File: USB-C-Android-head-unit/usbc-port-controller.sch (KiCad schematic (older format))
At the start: 5 parts

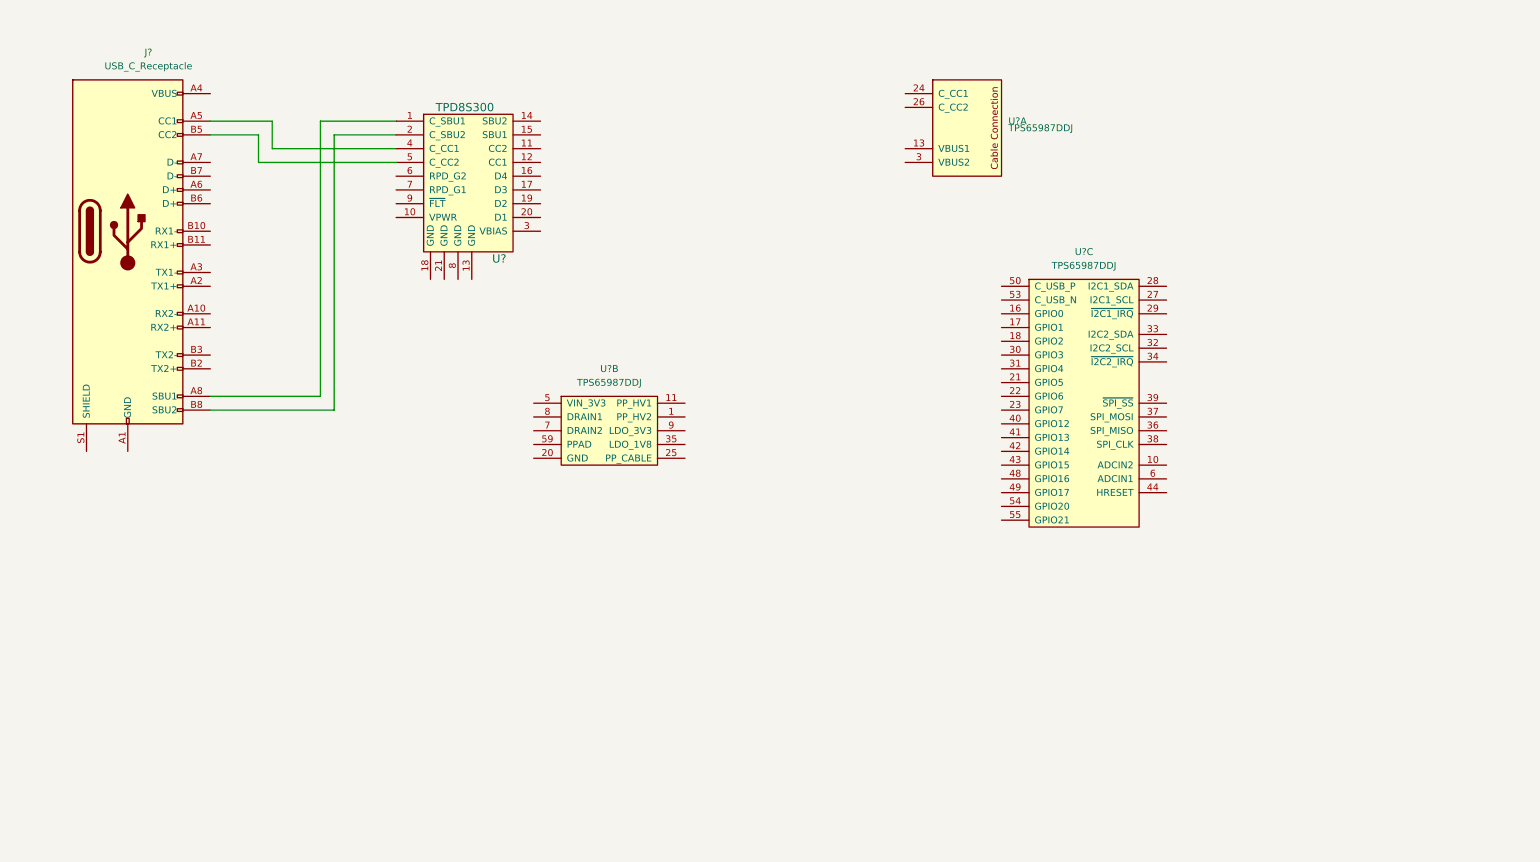
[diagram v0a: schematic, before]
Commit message: starting usb c design
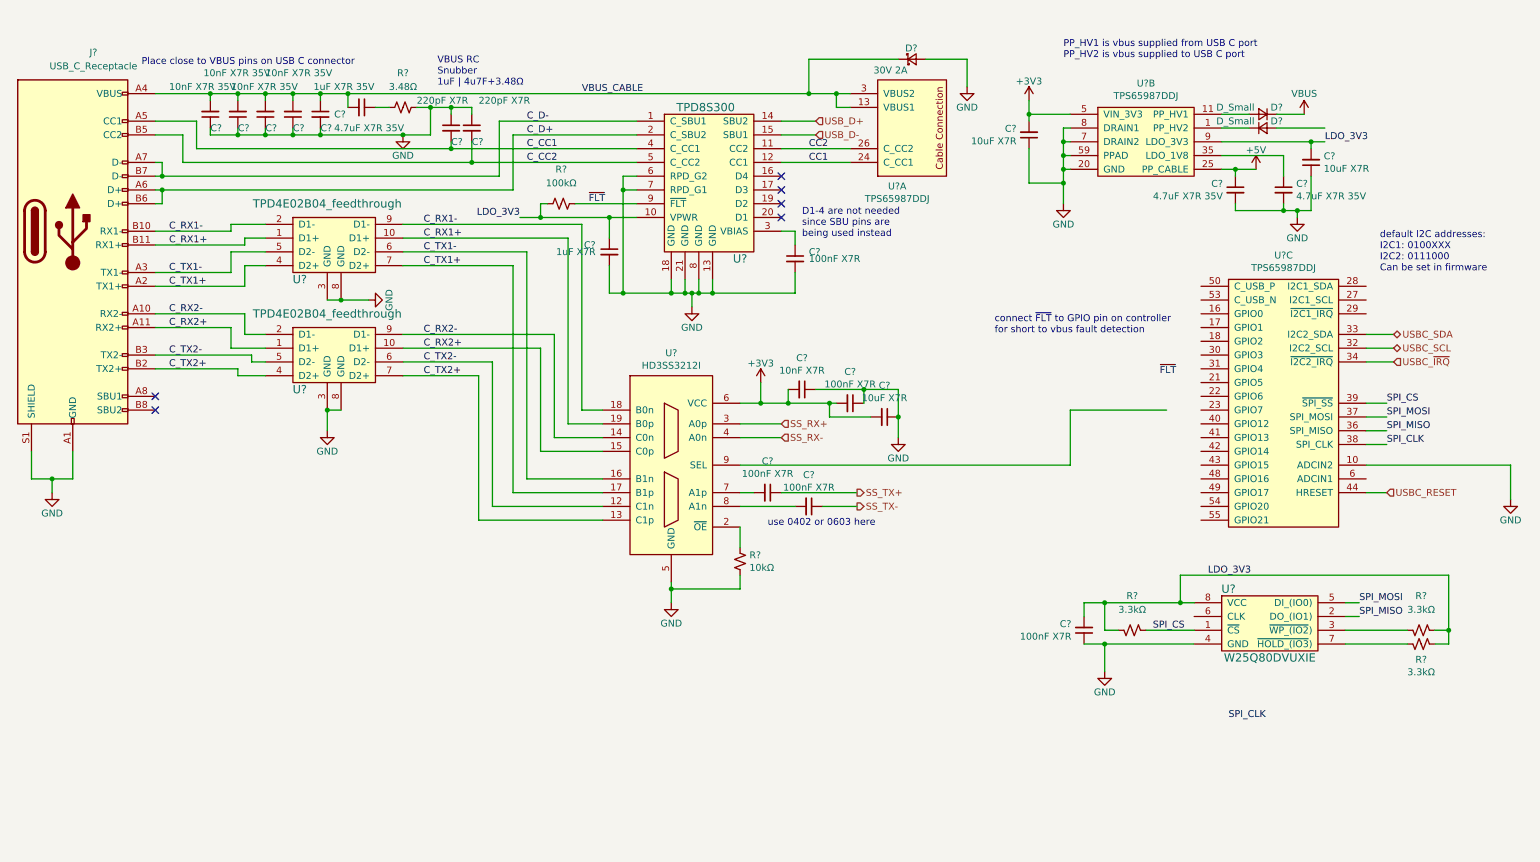
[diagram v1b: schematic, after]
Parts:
- added C? (x5): 100nF X7R, symbol Device:C_Small
- added C?: 1uF X7R, symbol Device:C_Small
- added C?: 10nF X7R, symbol Device:C_Small
- added C? (x3): 10uF X7R, symbol Device:C_Small
- added C? (x4): 10nF X7R 35V, symbol Device:C_Small
- added C?: 1uF X7R 35V, symbol Device:C_Small
- added C? (x3): 4.7uF X7R 35V, symbol Device:C_Small
- added C? (x2): 220pF X7R, symbol Device:C_Small
- added D? (x2): D_Small, symbol Device:D_Small
- added D?: 30V 2A, symbol Device:D_Schottky_Small
- added R?: 100kΩ, symbol Device:R_Small_US
- added R?: 10kΩ, symbol Device:R_Small_US
- added R?: 3.48Ω, symbol Device:R_Small_US
- added R? (x3): 3.3kΩ, symbol Device:R_Small_US
- added U? (x2): TPD4E02B04_feedthrough, Package_SON:USON-10_2.5x1.0mm_P0.5mm, symbol SW-Texas:TPD4E02B04_feedthrough
- added U?: HD3SS3212I, symbol SW-Texas:HD3SS3212I
- added U?: W25Q80DVUXIE, Package_SON:SON-8-1EP_3x2mm_P0.5mm_EP1.4x1.6mm, symbol SW-Winbond:W25Q80DVUXIE
- J?: MPN (none) -> UJ31-CH-3-SMT-TR; Manufacturer (none) -> CUI Inc
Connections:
- net GND: now reaches J?.A1 (GND), J?.A12 (GND), J?.B1 (GND), J?.B12 (GND)
- net GND: now also J?.S1 (SHIELD), U?.10 (ADCIN2), U?.13 (GND), U?.15 (DRAIN1), U?.18 (GND), U?.19 (DRAIN1), U?.20 (GND), U?.21 (GND), U?.45 (GND), U?.46 (GND), U?.47 (GND), U?.51 (GND), U?.52 (DRAIN2), U?.56 (DRAIN2), U?.57 (DRAIN2), U?.58 (DRAIN1), U?.59 (PPAD), U?.6 (RPD_G2), U?.7 (DRAIN2), U?.7 (RPD_G1), U?.8 (DRAIN1), U?.8 (GND), C?.1, C?.1, C?.1, C?.1, C?.1, C?.1, C?.1, C?.1, C?.1, C?.1, C?.1, C?.1, C?.2, C?.2, C?.2, C?.2, C?.2, D?.2 (A), R?.2, R?.2, U?.11 (GND), U?.20 (GND), U?.3 (GND), U?.3 (GND), U?.4 (GND), U?.5 (GND), U?.8 (GND), U?.8 (GND)
- net C_RX2-: now reaches J?.A10 (RX2-)
- net C_RX2-: now also U?.14 (C0n), U?.2 (D1-), U?.9 (D1-)
- net C_RX2+: now reaches J?.A11 (RX2+)
- net C_RX2+: now also U?.1 (D1+), U?.10 (D1+), U?.15 (C0p)
- net C_TX1+: now reaches J?.A2 (TX1+)
- net C_TX1+: now also U?.17 (B1p), U?.4 (D2+), U?.7 (D2+)
- net C_TX1-: now reaches J?.A3 (TX1-)
- net C_TX1-: now also U?.16 (B1n), U?.5 (D2-), U?.6 (D2-)
- net VBUS_CABLE: now reaches J?.A4 (VBUS), J?.A9 (VBUS), J?.B4 (VBUS), J?.B9 (VBUS)
- net VBUS_CABLE: now also U?.13 (VBUS1), U?.14 (VBUS1), U?.3 (VBUS2), U?.4 (VBUS2), C?.1, C?.2, C?.2, C?.2, C?.2, C?.2, D?.1 (K)
- net C_CC1: now reaches J?.A5 (CC1), U?.4 (C_CC1)
- net C_CC1: now also C?.2
- net C_D+: now reaches J?.A6 (D+)
- net C_D+: now also J?.B6 (D+), U?.2 (C_SBU2)
- net C_D-: now reaches J?.A7 (D-)
- net C_D-: now also J?.B7 (D-), U?.1 (C_SBU1)
- net at J?.A8 (SBU1): no longer U?.1 (C_SBU1)
- net C_RX1-: now reaches J?.B10 (RX1-)
- net C_RX1-: now also U?.18 (B0n), U?.2 (D1-), U?.9 (D1-)
- net C_RX1+: now reaches J?.B11 (RX1+)
- net C_RX1+: now also U?.1 (D1+), U?.10 (D1+), U?.19 (B0p)
- net C_TX2+: now reaches J?.B2 (TX2+)
- net C_TX2+: now also U?.13 (C1p), U?.4 (D2+), U?.7 (D2+)
- net C_TX2-: now reaches J?.B3 (TX2-)
- net C_TX2-: now also U?.12 (C1n), U?.5 (D2-), U?.6 (D2-)
- net C_CC2: now reaches J?.B5 (CC2), U?.5 (C_CC2)
- net C_CC2: now also C?.2
- net at J?.B8 (SBU2): no longer U?.2 (C_SBU2)
- net CC1: now reaches U?.24 (C_CC1)
- net CC1: now also U?.12 (CC1)
- net CC2: now reaches U?.26 (C_CC2)
- net CC2: now also U?.11 (CC2)
- net at U?.1 (PP_HV2), U?.2 (PP_HV2): now also D?.1 (K)
- net at U?.11 (PP_HV1), U?.12 (PP_HV1): now also D?.2 (A)
- net +5V: now reaches U?.25 (PP_CABLE)
- net +5V: now also C?.1
- net at U?.35 (LDO_1V8): now also C?.1
- net +3V3: now reaches U?.5 (VIN_3V3)
- net +3V3: now also C?.2, C?.2, C?.2, C?.2, U?.6 (VCC)
- net LDO_3V3: now reaches U?.9 (LDO_3V3)
- net LDO_3V3: now also U?.10 (VPWR), C?.1, C?.2, C?.2, R?.1, R?.2, R?.2, R?.2, U?.8 (VCC)
- net USBC_SCL: now reaches U?.32 (I2C2_SCL)
- net USBC_SDA: now reaches U?.33 (I2C2_SDA)
- net USBC_~IRQ: now reaches U?.34 (~I2C2_IRQ)
- net SPI_MISO: now reaches U?.36 (SPI_MISO)
- net SPI_MISO: now also U?.2 (DO_(IO1))
- net SPI_MOSI: now reaches U?.37 (SPI_MOSI)
- net SPI_MOSI: now also U?.5 (DI_(IO0))
- net SPI_CLK: now reaches U?.38 (SPI_CLK)
- net SPI_CS: now reaches U?.39 (~SPI_SS)
- net SPI_CS: now also R?.2, U?.1 (~CS)
- net USBC_RESET: now reaches U?.44 (HRESET)
- net USB_D+: now reaches U?.14 (SBU2)
- net USB_D-: now reaches U?.15 (SBU1)
- net at U?.3 (VBIAS): now also C?.1
- net ~FLT: now reaches U?.9 (~FLT)
- net ~FLT: now also R?.1
- new net: R?.1, U?.2 (~OE)
- new net: C?.2, U?.7 (A1p)
- new net: C?.2, U?.8 (A1n)
- new net: C?.1, R?.1
- new net: R?.1, U?.3 (~WP_(IO2))
- new net: R?.1, U?.7 (~HOLD_(IO3))
- new net SS_RX+: U?.3 (A0p)
- new net SS_RX-: U?.4 (A0n)
- new net SS_TX+: C?.1
- new net SS_TX-: C?.1
- new net VBUS: D?.1 (K)
- no-connect marks 0 -> 6
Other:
- note added: "D1-4 are not needed \nsince SBU pins are\nbeing used instead"
- note added: "PP_HV1 is vbus supplied from USB C port\nPP_HV2 is vbus supplied to USB C port"
- note added: "Place close to VBUS pins on USB C connector"
- note added: "VBUS RC\nSnubber\n1uF | 4u7F+3.48Ω"
- note added: "connect ~FLT~ to GPIO pin on controller\nfor short to vbus fault detection"
- note added: "default I2C addresses:\nI2C1: 0100XXX\nI2C2: 0111000\nCan be set in firmware"
- note added: "use 0402 or 0603 here"
- moved on the sheet: J?, U?, U?A, U?B, U?C

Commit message: work on USB hub
Also changed sheet sizes
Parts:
- added C?: 100nF X7R, symbol Device:C_Small
- added U?: TS5USBC402, symbol SW-Texas:TS5USBC402
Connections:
- net +3V3: now also C?.2, U?.B1 (VCC)
- net C_D+: now also U?.A2 (D+); no longer J?.A6 (D+), J?.B6 (D+)
- net C_D-: now also U?.A3 (D-); no longer J?.A7 (D-), J?.B7 (D-)
- net GND: now also C?.1, U?.B3 (GND)
- net SPI_CLK: now also U?.6 (CLK)
- net ~FLT: now also U?.A4 (~FLT)
- net CON_Orientation_SEL: now reaches U?.9 (SEL)
- net CON_Orientation_SEL: now also U?.A1 (SEL1), U?.B2 (SEL2)
- net VBUS_IN: now reaches D?.2 (A)
- new net C_D1+: J?.A6 (D+), U?.C3 (D1+)
- new net C_D1-: J?.A7 (D-), U?.C4 (D1-)
- new net C_D2+: J?.B6 (D+), U?.C1 (D2+)
- new net C_D2-: J?.B7 (D-), U?.C2 (D2-)
- no-connect marks 6 -> 7
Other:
- note added: "Internal PD\non SEL1, SEL2\n~OE~"
- note added: "SEL=L:\nRX1/TX1\nSEL=H:\nRX2/TX2"
- note added: "USB 2.0 pins A7/A6 for TX1/RX1\norientation"
- moved on the sheet: C?, R?, U?
